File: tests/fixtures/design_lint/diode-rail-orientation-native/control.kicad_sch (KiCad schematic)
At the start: 1 part

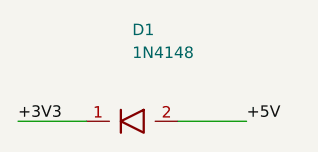
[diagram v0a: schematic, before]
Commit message: fix(design-lint): compare diode returns with positive rails
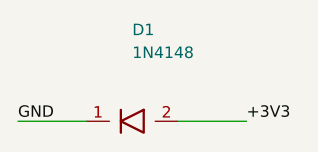
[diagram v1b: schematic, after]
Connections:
- net +5V is gone; now on net +3V3: D1.2 (A)
- net +3V3: no longer D1.1 (K)
- new net GND: D1.1 (K)
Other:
- title: Synthetic forward-oriented diode rail control -> Synthetic forward-oriented diode return control
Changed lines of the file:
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@@
 (kicad_sch (version 20231120) (generator "eeschema")
   (paper "A4")
-  (title_block (title "Synthetic forward-oriented diode rail control")
+  (title_block (title "Synthetic forward-oriented diode return control")
     (comment 1 "NOT FOR MANUFACTURE - tooling fixture"))
   (symbol (lib_id "Device:D") (at 63.50 63.50 0) (unit 1)
@@
     (stroke (width 0) (type default))
 )
-  (label "+3V3" (at 50.80 63.50 0)
+  (label "GND" (at 50.80 63.50 0)
     (effects (font (size 1.27 1.27)) (justify left bottom))
 )
@@
     (stroke (width 0) (type default))
 )
-  (label "+5V" (at 76.20 63.50 0)
+  (label "+3V3" (at 76.20 63.50 0)
     (effects (font (size 1.27 1.27)) (justify left bottom))
 )
